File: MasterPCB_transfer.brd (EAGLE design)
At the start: 279.4 x 330.2 mm, 982 parts, among them IC1 NCS21911SN2T1G, IC10 LDL1117S33R, IC11 LTC4222CUH#PBF, IC12 LTC4222CUH#PBF, IC13 LTC4222CUH#PBF, IC14 LTC4222CUH#PBF, IC15 LTC4222CUH#PBF, IC16 LTC4222CUH#PBF, IC17 LTC4222CUH#PBF, IC18 LTC4222CUH#PBF, IC19 LTC4222CUH#PBF, IC2 NCS21911SN2T1G, IC20 LTC4222CUH#PBF, IC21 LTC4222CUH#PBF, IC22 LTC4222CUH#PBF, IC23 LTC4222CUH#PBF, IC24 NCS21911SN2T1G, IC25 NCS21911SN2T1G, IC26 NCS21911SN2T1G, IC27 NCS21911SN2T1G, IC28 NCS21911SN2T1G, IC29 NCS21911SN2T1G, IC3 NCS21911SN2T1G, IC30 NCS21911SN2T1G, IC31 ADIS16500AMLZ, IC32 LTC6820IUD#PBF, IC33 CBTL01023GM,115, IC34 S35ML04G300WHI000, IC35 S35ML04G300WHI000, IC36 S35ML04G300WHI000, IC37 S35ML04G300WHI000, IC38 ADS8588HIPM, IC39 S35ML04G300WHI000, IC4 LTC4222CUH#PBF, IC40 S35ML04G300WHI000, IC41 S35ML04G300WHI000, IC42 S35ML04G300WHI000, IC43 S35ML04G300WHI000, IC44 S35ML04G300WHI000, IC45 S35ML04G300WHI000, IC46 S35ML04G300WHI000, IC47 S35ML04G300WHI000, IC48 S35ML04G300WHI000, IC49 S35ML04G300WHI000, IC5 LP38692SDX-5.0_NOPB, IC50 S35ML04G300WHI000, IC51 ADS8588HIPM, IC52 ADS8588HIPM, IC55 MUX36S16IRSNR, IC6 LP38692SDX-5.0_NOPB, IC7 LDL1117S33R, IC8 LDL1117S33R, IC9 LP38692SDX-5.0_NOPB, J1 SAMTEC-SMM-104-02-X-DJ, J2 SAMTEC-CLP-106-02-X-DJ, J3 SSM-109-L-SV, J4 TFM-120-02-L-D, J5 TFM-120-02-L-D, J6 TFM-120-02-L-D, J7 TFM-120-02-L-D, J8 TFM-120-02-L-D, M1 NTLUS4C12NTAG, M10 NTLUS4C12NTAG, M11 NTLUS4C12NTAG, M12 NTLUS4C12NTAG, M13 NTLUS4C12NTAG, M14 NTLUS4C12NTAG, M15 NTLUS4C12NTAG, M16 NTLUS4C12NTAG, M17 NTLUS4C12NTAG, M18 NTLUS4C12NTAG, M19 NTLUS4C12NTAG, M2 NTLUS4C12NTAG, M20 NTLUS4C12NTAG, M21 NTLUS4C12NTAG, M22 NTLUS4C12NTAG, M23 NTLUS4C12NTAG, M24 NTLUS4C12NTAG, M25 NTLUS4C12NTAG, M26 NTLUS4C12NTAG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

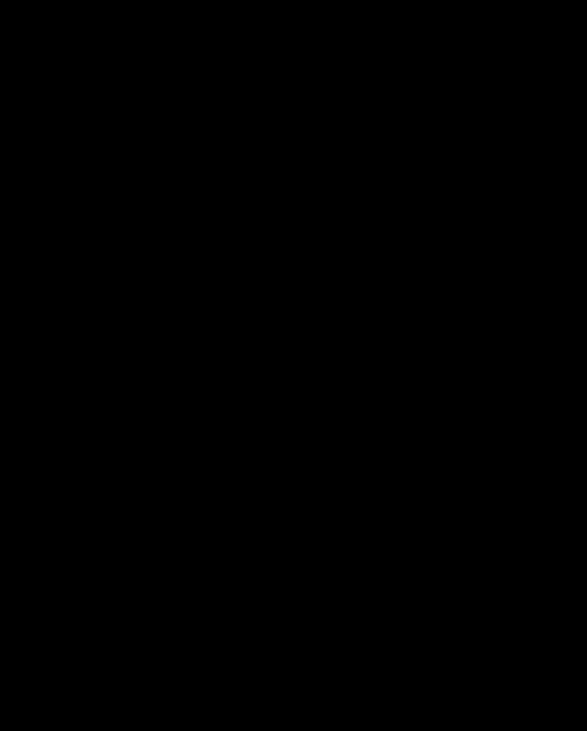
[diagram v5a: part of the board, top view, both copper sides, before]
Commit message: Schematic done, ready for review, only needs com LED and test point, waiting till after routing to see if there is enough space to add extra hardware
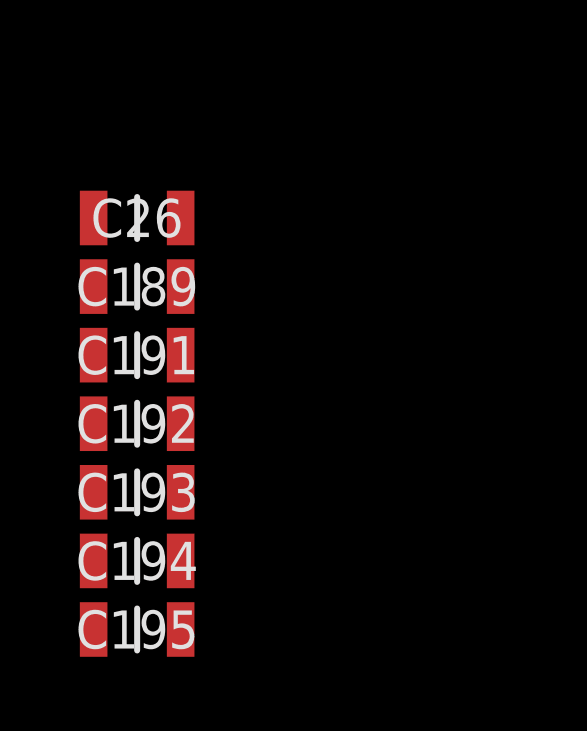
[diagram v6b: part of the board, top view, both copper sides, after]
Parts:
- added C189, C191, C192, C193, C194, C195, C26: GRM31C5C1E474JE01L, SamacSys_Parts:CAPC3216X180N
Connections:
- removed net GP_6_N: IC52.60
- removed net GP_7_N: IC52.62
- removed net GP_8_N: IC52.64
- net 13.5V_BUS: now also C189.1, C191.1, C192.1, C193.1, C194.1, C195.1, C26.1
- net GND: now also C189.2, C191.2, C192.2, C193.2, C194.2, C195.2, C26.2, IC52.60, IC52.62, IC52.64

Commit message: Smashing font
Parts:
- removed C111: CNA5L1X7R1C106K160AE, SamacSys_Parts:CAPC3216X180N
- removed F1, F10, F11, F12, F2, F3, F4, F5, F6, F7, F8, F9: RTR025N05HZGTL, SamacSys_Parts:SOT95P280X110-3N
- added C196: CGA4J3X7R1H105K125AB, SamacSys_Parts:CAPC2012X145N
- added D45, D48, D75, D78, D79, D80, D81, D82, D84, D85, D86, D87: RSR025N03HZGTL, SamacSys_Parts:SOT95P280X100-3N
- C1, C13, C16, C17, C22, C25: value C3225X7R1N106K250AC -> C3216X7R1E106K160AE; device SamacSys_Parts:CAPC3225X230N -> SamacSys_Parts:C3216_COMMERCIAL
- C100, C102, C103, C104, C105, C106, C108, C109, C110, C96, C98: value CNA5L1X7R1C106K160AE -> C3216X7R1E106K160AE; device SamacSys_Parts:CAPC3216X180N -> SamacSys_Parts:C3216_COMMERCIAL
- C19, C20, C21, C23, C24: value 06033C105KAT4A -> CGA4J3X7R1H105K125AB; device SamacSys_Parts:CAPC1608X90N -> SamacSys_Parts:CAPC2012X145N
- C27: value 06033C105KAT4A -> C3216X7R1E106K160AE; device SamacSys_Parts:CAPC1608X90N -> SamacSys_Parts:C3216_COMMERCIAL
- moved C189 1313.9 mm to (-317.3, 678.0)
- moved C191 1313.9 mm to (-317.3, 675.7)
- moved C192 1313.9 mm to (-317.3, 673.4)
- moved C193 1313.9 mm to (-317.3, 671.1)
- moved C194 1313.9 mm to (-317.3, 668.9)
- moved C195 1313.9 mm to (-317.3, 666.6)
- moved C26 1313.9 mm to (-317.3, 680.3)
- moved C19 1177.7 mm to (-324.1, 655.1)
- moved C20 1169.6 mm to (-324.1, 648.2)
- moved C21 1161.7 mm to (-324.1, 641.2)
- moved R41 1155.4 mm to (-239.5, 619.2)
- moved R46 1155.4 mm to (-258.6, 581.1)
- moved R51 1155.4 mm to (-254.8, 619.2)
- moved C23 1146.7 mm to (-324.1, 627.4)
- moved C24 1139.5 mm to (-324.1, 620.5)
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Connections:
- net 3.3V_DIGITAL: now also C105.2, C196.2; no longer C110.1, C24.2
- net 3.3V_SENSORS: now also C106.2; no longer C104.1
- net 3.3V_SWITCHING: now also C110.2; no longer C103.1
- net 5V_BUS: now also C104.2, C108.2, C109.2; no longer C105.1, C106.1, C111.1
- net 5V_CONNECTOR: now also C103.2; no longer C109.1
- net 5V_MCU: now also C96.2; no longer C98.1
- net 5V_ON_BOARD: now also C100.2, C24.2; no longer C102.1, C27.2
- net 6.5V_BUS: now also C102.2, C27.2, C98.2; no longer C100.1, C108.1, C96.1
- net D_SENSE1: now also D45.3; no longer F2.3
- net D_SENSE2: now also D48.3; no longer F1.3
- net D_SENSE3: now also D75.3; no longer F3.3
- net D_SENSE4: now also D78.3; no longer F4.3
- net D_SENSE5: now also D79.3; no longer F6.3
- net D_SENSE6: now also D80.3; no longer F7.3
- net D_SENSE7: now also D81.3; no longer F8.3
- net D_SENSE8: now also D82.3; no longer F9.3
- net GND: now also C100.1, C102.1, C103.1, C104.1, C105.1, C106.1, C108.1, C109.1, C110.1, C196.1, C96.1, C98.1, D45.2, D48.2, D75.2, D78.2, D79.2, D80.2, D81.2, D82.2, D84.2, D85.2, D86.2, D87.2; no longer C100.2, C102.2, C103.2, C104.2, C105.2, C106.2, C108.2, C109.2, C110.2, C111.2, C96.2, C98.2, F1.2, F10.2, F11.2, F12.2, F2.2, F3.2, F4.2, F5.2, F6.2, F7.2, F8.2, F9.2
- net N$112: now also D84.3; no longer F5.3
- net N$113: now also D84.1; no longer F5.1
- net N$116: now also D75.1; no longer F3.1
- net N$118: now also D85.3; no longer F10.3
- net N$120: now also D78.1; no longer F4.1
- net N$122: now also D85.1; no longer F10.1
- net N$128: now also D86.3; no longer F11.3
- net N$131: now also D86.1; no longer F11.1
- net N$135: now also D87.3; no longer F12.3
- net N$137: now also D79.1; no longer F6.1
- net N$138: now also D87.1; no longer F12.1
- net N$140: now also D80.1; no longer F7.1
- net N$143: now also D81.1; no longer F8.1
- net N$146: now also D82.1; no longer F9.1
- net N$19: now also D48.1; no longer F1.1
- net N$22: now also D45.1; no longer F2.1
- net REFCAPAB0: now also C16.1; no longer C22.1
- net REFCAPAB00: now also C17.1; no longer C25.1
- net REFIN/OUT0: now also C22.1; no longer C16.1
- net REFIN/OUT00: now also C25.1; no longer C17.1

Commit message: Created BareBoardLayout for preliminary enclosure design
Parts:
- removed J3: SSM-109-L-SV, SamacSys_Parts:SAMTEC_SSM-109-L-SV
- added J9: SSM-109-L-SV, SamacSys_Parts:SAMTEC_SSM-109-L-SV
- moved C174 735.1 mm to (290.8, 111.8)
- moved C176 735.1 mm to (290.8, 147.4)
- moved C177 735.1 mm to (290.8, 210.9)
- moved C178 735.1 mm to (290.8, 213.4)
- moved C179 735.1 mm to (290.8, 216.0)
- moved C180 735.1 mm to (290.8, 218.5)
- moved C181 735.1 mm to (290.8, 282.0)
- moved C182 735.1 mm to (311.1, 282.0)
- moved C183 735.1 mm to (290.8, 284.5)
- moved C184 735.1 mm to (311.1, 284.5)
- moved C187 735.1 mm to (290.8, 289.6)
- moved C188 735.1 mm to (311.1, 289.6)
- moved IC35 735.1 mm to (283.2, 100.4)
- moved IC36 735.1 mm to (283.2, 118.2)
- moved IC37 735.1 mm to (283.2, 135.9)
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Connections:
- net 13.5V_BUS: now also J6.32
- net 14V_BUS_FROM_CONNECTOR: no longer J6.32
- net 3.3V_NC: now also J9.09; no longer J3.01
- net 3.3V_SENSORS: now also J9.02; no longer J3.08
- net 5V_BUS: now also J6.28
- net 5V_BUS_FROM_CONNECTOR: no longer J6.28
- net 6.5V_BUS: now also J6.30
- net 6.5V_BUS_FROM_CONNECTOR: no longer J6.30
- net FIX_NC: now also J9.06; no longer J3.04
- net GND: now also J9.03; no longer J3.07
- net GPS_EN: now also J9.08; no longer J3.02
- net GPS_RX: now also J9.04; no longer J3.06
- net GPS_TX: now also J9.05; no longer J3.05
- net PPS_NC: now also J9.01; no longer J3.09
- net VBAT_NC: now also J9.07; no longer J3.03
